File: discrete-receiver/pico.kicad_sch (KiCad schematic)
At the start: 44 parts, among them SW1 Reset, U12 TPS7A20xxxDBV, U13 LM66100DCK, U14 LM66100DCK, U15 LM66100DCK, U6 RP2350A, U7 W25Q128JVS, U8 NCP1117-3.3_SOT223, Y1 ABM8-272-T3

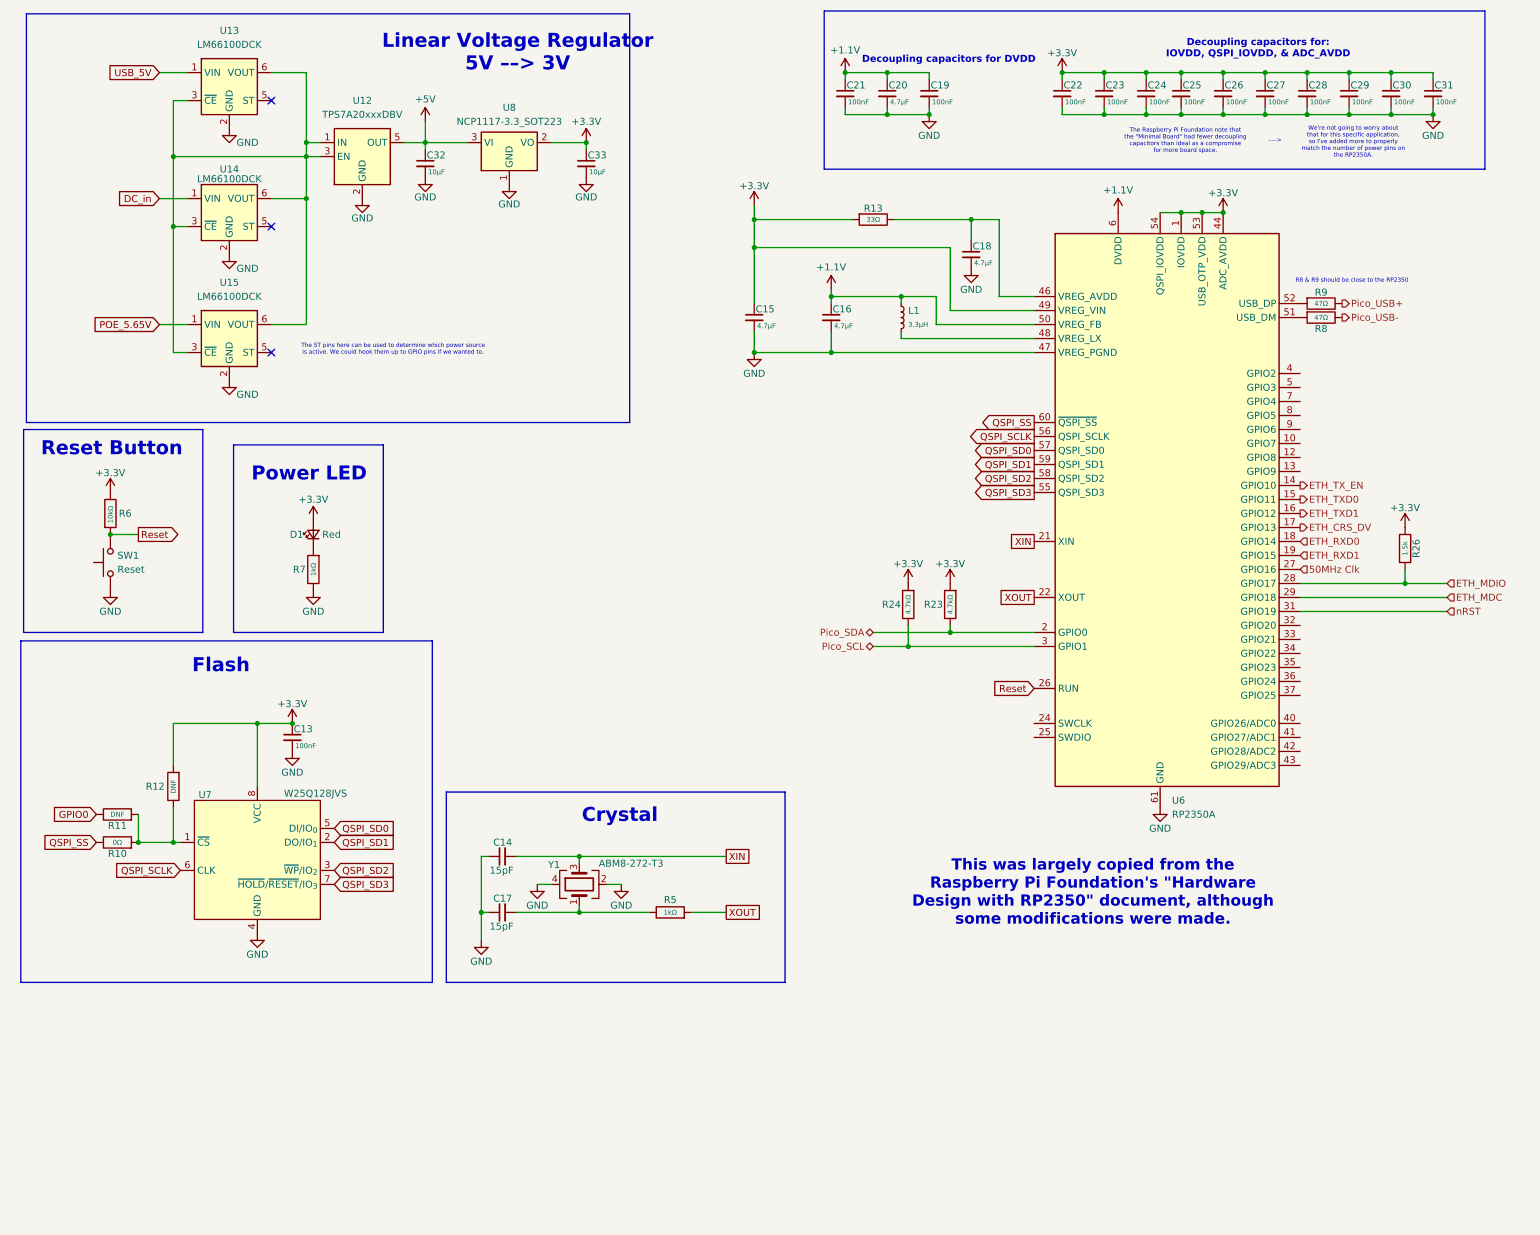
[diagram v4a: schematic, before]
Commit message: Organized Schematic
Standardized component labelling and font sizes. Added descriptions to some sub sheets and organized layout of root sheet.
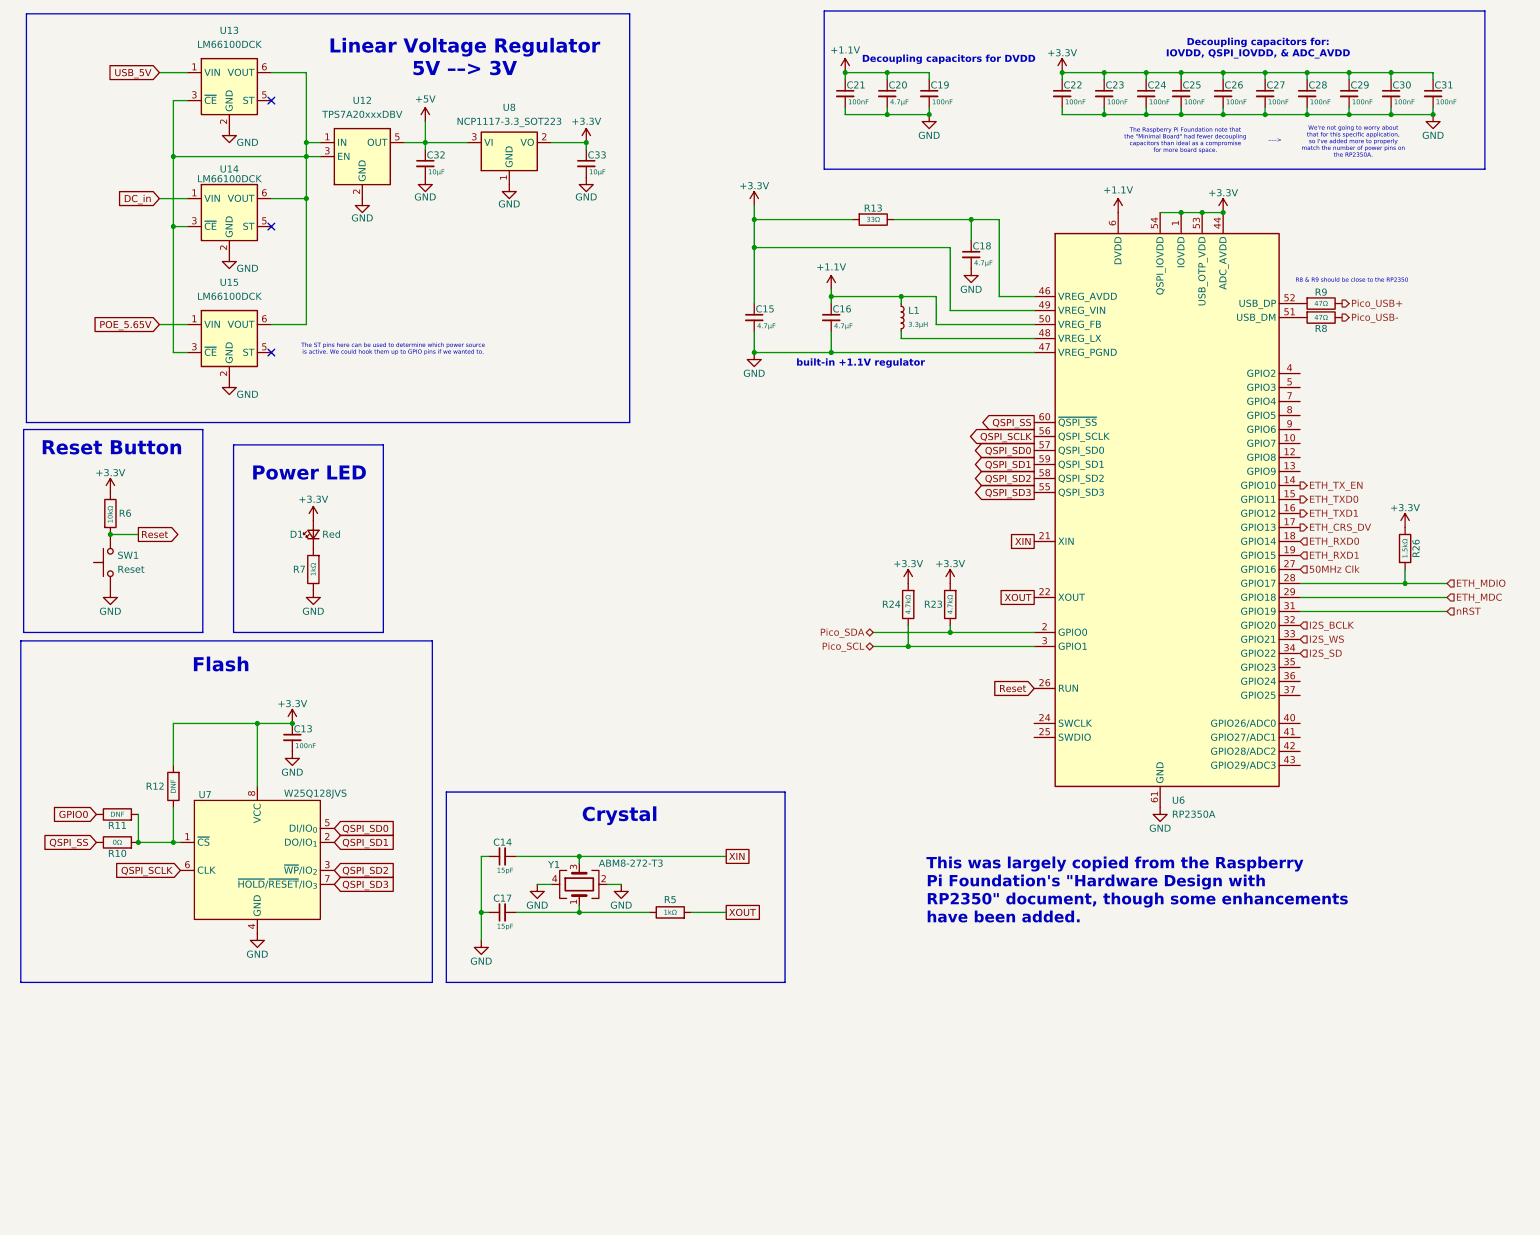
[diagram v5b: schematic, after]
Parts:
- R26: value 1.5k -> 1.5kΩ
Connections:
- net I2S_BCLK: now reaches U6.32 (GPIO20)
- net I2S_WS: now reaches U6.33 (GPIO21)
- net I2S_SD: now reaches U6.34 (GPIO22)
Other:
- note added: "This was largely copied from the Raspberry Pi Foundation's "Hardware Design with RP2350" document, though some enhancements have been added."
- note added: "built-in +1.1V regulator"
- note removed: "This was largely copied from the Raspberry Pi Foundation's "Hardware Design with RP2350" document, although some modifications were made."
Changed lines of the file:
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@@
 		)
 	)
+	(text "built-in +1.1V regulator "
+		(exclude_from_sim no)
+		(at 166.624 78.232 0)
+		(effects
+			(font
+				(size 1.27 1.27)
+				(thickness 0.254)
+				(bold yes)
+			)
+		)
+	)
 	(text "Decoupling capacitors for DVDD"
 		(exclude_from_sim no)
@@
 		)
 	)
-	(text "This was largely copied from the \nRaspberry Pi Foundation's \"Hardware \nDesign with RP2350\" document, although\nsome modifications were made."
+	(text "This was largely copied from the Raspberry\nPi Foundation's \"Hardware Design with \nRP2350\" document, though some enhancements\nhave been added."
 		(exclude_from_sim no)
-		(at 208.788 174.244 0)
+		(at 178.562 173.99 0)
 		(effects
 			(font
 				(size 2.032 2.032)
-				(thickness 0.254)
+				(thickness 0.4064)
 				(bold yes)
 			)
+			(justify left)
 		)
 	)
@@
 	(text "Linear Voltage Regulator\n5V ––> 3V"
 		(exclude_from_sim no)
-		(at 104.394 21.844 0)
+		(at 94.742 22.86 0)
 		(effects
 			(font
@@
 		)
 	)
+	(hierarchical_label "I2S_WS"
+		(shape input)
+		(at 246.38 128.27 0)
+		(effects
+			(font
+				(size 1.27 1.27)
+			)
+			(justify left)
+		)
+	)
 	(hierarchical_label "nRST"
 		(shape input)
@@
 		)
 	)
+	(hierarchical_label "I2S_SD"
+		(shape input)
+		(at 246.38 130.81 0)
+		(effects
+			(font
+				(size 1.27 1.27)
+			)
+			(justify left)
+		)
+	)
 	(hierarchical_label "ETH_RXD1"
 		(shape input)
@@
 		)
 	)
+	(hierarchical_label "I2S_BCLK"
+		(shape input)
+		(at 246.38 125.73 0)
+		(effects
+			(font
+				(size 1.27 1.27)
+			)
+			(justify left)
+		)
+	)
 	(hierarchical_label "ETH_RXD0"
 		(shape input)
@@
 			(effects
 				(font
-					(size 1.27 1.27)
+					(size 0.889 0.889)
 				)
 				(justify left)
@@
 			)
 		)
-		(property "Value" "1.5k"
+		(property "Value" "1.5kΩ"
 			(at 265.43 111.76 90)
 			(show_name no)
@@
 			(effects
 				(font
-					(size 1.27 1.27)
+					(size 0.889 0.889)
 				)
 				(justify left)

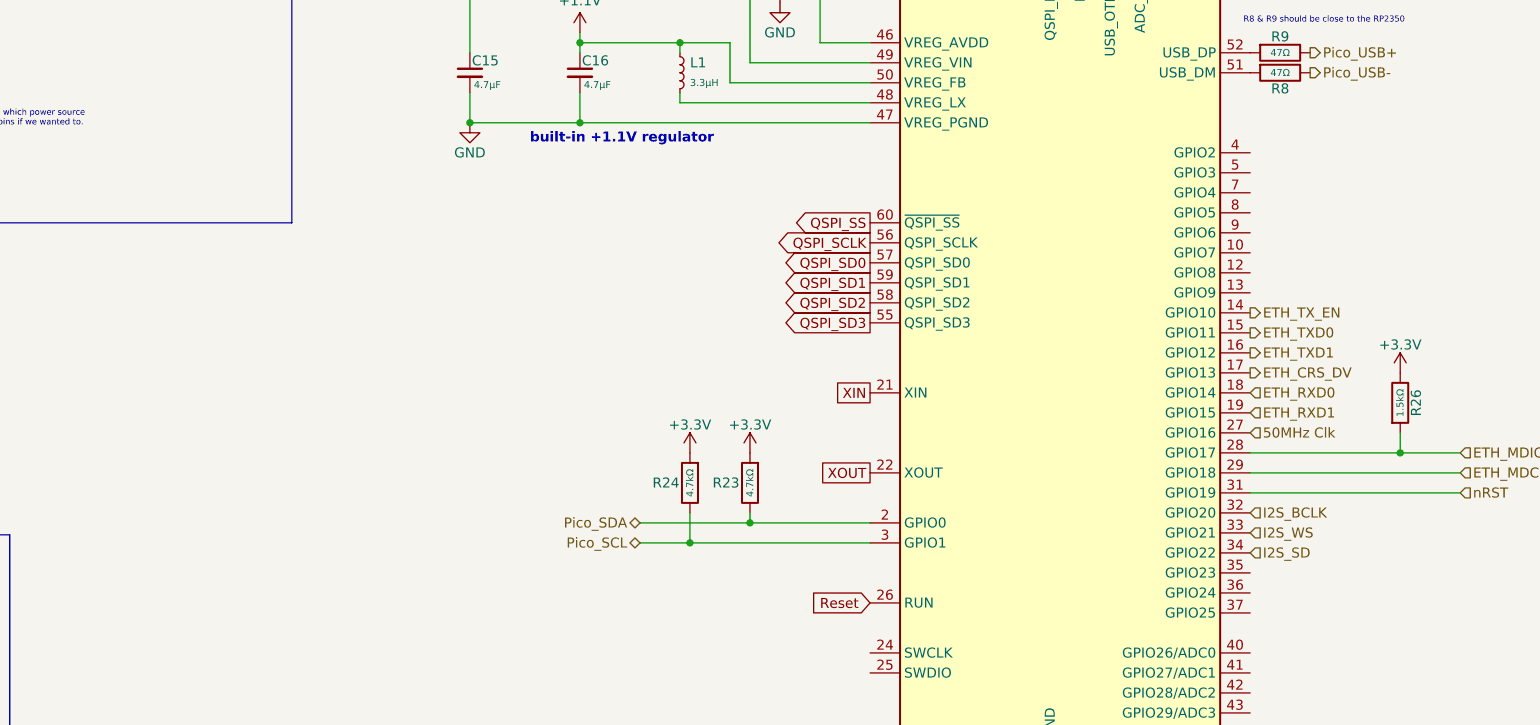
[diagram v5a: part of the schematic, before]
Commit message: Updated ethernet clocking details
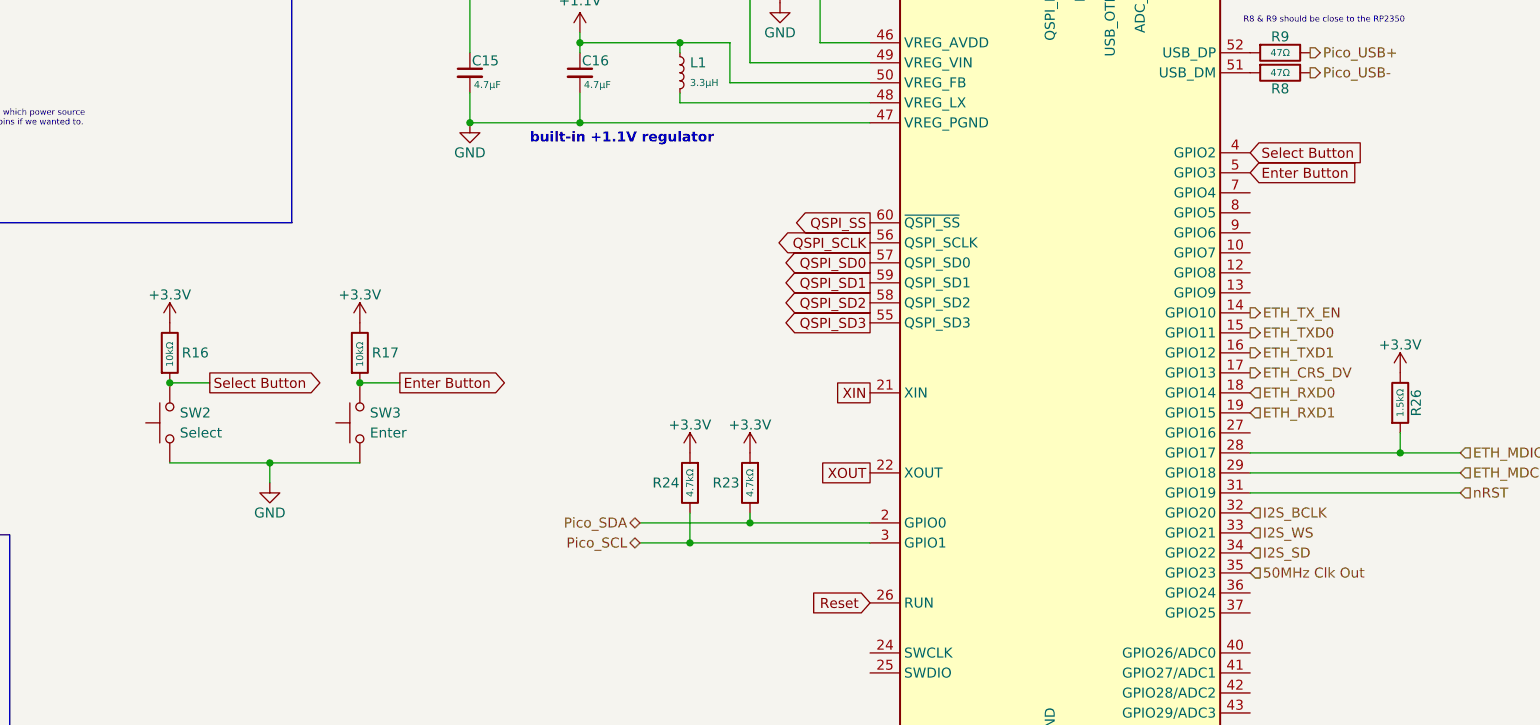
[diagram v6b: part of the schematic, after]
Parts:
- added R16, R17: 10kΩ, symbol Device:R
- added SW2: Select, symbol Switch:SW_Push
- added SW3: Enter, symbol Switch:SW_Push
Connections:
- net +3.3V: now also R16.1, R17.1
- net GND: now also SW2.1, SW3.1
- net 50MHz Clk Out: now reaches U6.35 (GPIO23)
- net Select Button: now reaches U6.4 (GPIO2)
- net Select Button: now also R16.2, SW2.2
- net Enter Button: now reaches U6.5 (GPIO3)
- net Enter Button: now also R17.2, SW3.2
- net 50MHz Clk: no longer names the net of U6.27 (GPIO16)
